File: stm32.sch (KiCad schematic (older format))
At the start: 35 parts, among them J10 Micro_SD_Card, J16 Conn_02x20_Odd_Even, P2 CONN_01X04, U3 STM32F407VETx, U4 USBLC6-4SC6, Y2 25M, Y3 RTC

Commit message: add bodge pads and move stuff around
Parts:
- added TP1, TP10, TP11, TP2, TP3, TP4, TP5, TP6, TP7, TP8, TP9: TestPoint, TestPoint:TestPoint_Pad_D1.0mm, symbol Connector:TestPoint
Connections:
- net at U3.55 (PD8): now also TP3.1
- net at U3.56 (PD9): now also TP4.1
- net at U3.57 (PD10): now also TP5.1
- net at U3.58 (PD11): now also TP6.1
- net at U3.59 (PD12): now also TP7.1
- net at U3.61 (PD14): now also TP8.1
- net at U3.62 (PD15): now also TP9.1
- net at U3.63 (PC6): now also TP10.1
- net at U3.64 (PC7): now also TP11.1
- net at U3.68 (PA9): now also TP1.1
- net at U3.69 (PA10): now also TP2.1
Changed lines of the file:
@@
 	8700 1500 8750 1500
-$Comp
-L stmbl:STM32F40xV U3
-U 1 1 57A8F89A
-P 10100 3950
-F 0 "U3" H 10850 1200 50  0000 C CNN
-F 1 "STM32F407VETx" H 10100 3950 50  0000 C CNN
-F 2 "stmbl:LQFP-100_14x14mm_Pitch0.5mm" H 10100 3100 50  0001 C CNN
-F 3 "" H 10100 3950 50  0000 C CNN
-F 4 "" H 0   0   50  0001 C CNN "Manufacturer No"
-F 5 "" H 0   0   50  0001 C CNN "Source"
-F 6 "" H 0   0   50  0001 C CNN "Tolerance"
-F 7 "" H 0   0   50  0001 C CNN "Voltage"
-	1    10100 3950
-	1    0    0    -1
-$EndComp
 $Comp
 L stmbl:C C46
@@
 	1    0    0    -1
 $EndComp
+$Comp
+L stmbl:STM32F40xV U3
+U 1 1 57A8F89A
+P 10100 3950
+F 0 "U3" H 10850 1200 50  0000 C CNN
+F 1 "STM32F407VETx" H 10100 3950 50  0000 C CNN
+F 2 "stmbl:LQFP-100_14x14mm_Pitch0.5mm" H 10100 3100 50  0001 C CNN
+F 3 "" H 10100 3950 50  0000 C CNN
+F 4 "" H 0   0   50  0001 C CNN "Manufacturer No"
+F 5 "" H 0   0   50  0001 C CNN "Source"
+F 6 "" H 0   0   50  0001 C CNN "Tolerance"
+F 7 "" H 0   0   50  0001 C CNN "Voltage"
+	1    10100 3950
+	1    0    0    -1
+$EndComp
+$Comp
+L Connector:TestPoint TP3
+U 1 1 5D2700EF
+P 11400 4000
+F 0 "TP3" V 11354 4188 50  0000 L CNN
+F 1 "TestPoint" V 11400 4300 50  0000 L CNN
+F 2 "TestPoint:TestPoint_Pad_D1.0mm" H 11600 4000 50  0001 C CNN
+F 3 "~" H 11600 4000 50  0001 C CNN
+	1    11400 4000
+	0    1    1    0
+$EndComp
+Wire Wire Line
+	11250 4000 11400 4000
+$Comp
+L Connector:TestPoint TP4
+U 1 1 5D2704C1
+P 11400 4100
+F 0 "TP4" V 11354 4288 50  0000 L CNN
+F 1 "TestPoint" V 11400 4400 50  0000 L CNN
+F 2 "TestPoint:TestPoint_Pad_D1.0mm" H 11600 4100 50  0001 C CNN
+F 3 "~" H 11600 4100 50  0001 C CNN
+	1    11400 4100
+	0    1    1    0
+$EndComp
+Wire Wire Line
+	11250 4100 11400 4100
+$Comp
+L Connector:TestPoint TP5
+U 1 1 5D270727
+P 11400 4200
+F 0 "TP5" V 11354 4388 50  0000 L CNN
+F 1 "TestPoint" V 11400 4500 50  0000 L CNN
+F 2 "TestPoint:TestPoint_Pad_D1.0mm" H 11600 4200 50  0001 C CNN
+F 3 "~" H 11600 4200 50  0001 C CNN
+	1    11400 4200
+	0    1    1    0
+$EndComp
+Wire Wire Line
+	11250 4200 11400 4200
+$Comp
+L Connector:TestPoint TP6
+U 1 1 5D2709E1
+P 11400 4300
+F 0 "TP6" V 11354 4488 50  0000 L CNN
+F 1 "TestPoint" V 11400 4600 50  0000 L CNN
+F 2 "TestPoint:TestPoint_Pad_D1.0mm" H 11600 4300 50  0001 C CNN
+F 3 "~" H 11600 4300 50  0001 C CNN
+	1    11400 4300
+	0    1    1    0
+$EndComp
+Wire Wire Line
+	11250 4300 11400 4300
+$Comp
+L Connector:TestPoint TP7
+U 1 1 5D270C47
+P 11400 4400
+F 0 "TP7" V 11354 4588 50  0000 L CNN
+F 1 "TestPoint" V 11400 4700 50  0000 L CNN
+F 2 "TestPoint:TestPoint_Pad_D1.0mm" H 11600 4400 50  0001 C CNN
+F 3 "~" H 11600 4400 50  0001 C CNN
+	1    11400 4400
+	0    1    1    0
+$EndComp
+Wire Wire Line
+	11250 4400 11400 4400
+$Comp
+L Connector:TestPoint TP8
+U 1 1 5D270E75
+P 11400 4600
+F 0 "TP8" V 11354 4788 50  0000 L CNN
+F 1 "TestPoint" V 11400 4900 50  0000 L CNN
+F 2 "TestPoint:TestPoint_Pad_D1.0mm" H 11600 4600 50  0001 C CNN
+F 3 "~" H 11600 4600 50  0001 C CNN
+	1    11400 4600
+	0    1    1    0
+$EndComp
+Wire Wire Line
+	11250 4600 11400 4600
+$Comp
+L Connector:TestPoint TP9
+U 1 1 5D2710F7
+P 11400 4700
+F 0 "TP9" V 11354 4888 50  0000 L CNN
+F 1 "TestPoint" V 11400 5000 50  0000 L CNN
+F 2 "TestPoint:TestPoint_Pad_D1.0mm" H 11600 4700 50  0001 C CNN
+F 3 "~" H 11600 4700 50  0001 C CNN
+	1    11400 4700
+	0    1    1    0
+$EndComp
+Wire Wire Line
+	11250 4700 11400 4700
+$Comp
+L Connector:TestPoint TP10
+U 1 1 5D27230B
+P 11400 5600
+F 0 "TP10" V 11354 5788 50  0000 L CNN
+F 1 "TestPoint" V 11400 5900 50  0000 L CNN
+F 2 "TestPoint:TestPoint_Pad_D1.0mm" H 11600 5600 50  0001 C CNN
+F 3 "~" H 11600 5600 50  0001 C CNN
+	1    11400 5600
+	0    1    1    0
+$EndComp
+Wire Wire Line
+	11250 5600 11400 5600
+$Comp
+L Connector:TestPoint TP11
+U 1 1 5D2727D7
+P 11400 5700
+F 0 "TP11" V 11354 5888 50  0000 L CNN
+F 1 "TestPoint" V 11400 6000 50  0000 L CNN
+F 2 "TestPoint:TestPoint_Pad_D1.0mm" H 11600 5700 50  0001 C CNN
+F 3 "~" H 11600 5700 50  0001 C CNN
+	1    11400 5700
+	0    1    1    0
+$EndComp
+Wire Wire Line
+	11250 5700 11400 5700
+$Comp
+L Connector:TestPoint TP1
+U 1 1 5D272AB9
+P 8800 4100
+F 0 "TP1" V 8754 4288 50  0000 L CNN
+F 1 "TestPoint" V 8800 4400 50  0000 L CNN
+F 2 "TestPoint:TestPoint_Pad_D1.0mm" H 9000 4100 50  0001 C CNN
+F 3 "~" H 9000 4100 50  0001 C CNN
+	1    8800 4100
+	0    -1   -1   0
+$EndComp
+Wire Wire Line
+	8950 4100 8800 4100
+$Comp
+L Connector:TestPoint TP2
+U 1 1 5D272FE7
+P 8800 4200
+F 0 "TP2" V 8754 4388 50  0000 L CNN
+F 1 "TestPoint" V 8800 4500 50  0000 L CNN
+F 2 "TestPoint:TestPoint_Pad_D1.0mm" H 9000 4200 50  0001 C CNN
+F 3 "~" H 9000 4200 50  0001 C CNN
+	1    8800 4200
+	0    -1   -1   0
+$EndComp
+Wire Wire Line
+	8950 4200 8800 4200
 $EndSCHEMATC

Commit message: fix SD card socket, move around psu stuff
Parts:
- J10: footprint Connector_Card:microSD_HC_Hirose_DM3D-SF -> Connector_Card:microSD_HC_Hirose_DM3BT-DSF-PEJS
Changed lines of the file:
@@
 EESchema Schematic File Version 5
 LIBS:powermetering-cache
-EELAYER 29 0
+EELAYER 30 0
 EELAYER END
 $Descr A3 16535 11693
@@
 Comment3 ""
 Comment4 ""
+Comment5 ""
+Comment6 ""
+Comment7 ""
+Comment8 ""
+Comment9 ""
 $EndDescr
 Text HLabel 7850 3400 0    60   Input ~ 0
@@
 F 0 "J10" H 13500 6217 50  0000 C CNN
 F 1 "Micro_SD_Card" H 13500 6126 50  0000 C CNN
-F 2 "Connector_Card:microSD_HC_Hirose_DM3D-SF" H 14700 5800 50  0001 C CNN
+F 2 "Connector_Card:microSD_HC_Hirose_DM3BT-DSF-PEJS" H 14700 5800 50  0001 C CNN
 F 3 "http://katalog.we-online.de/em/datasheet/693072010801.pdf" H 13550 5500 50  0001 C CNN
 	1    13550 5500

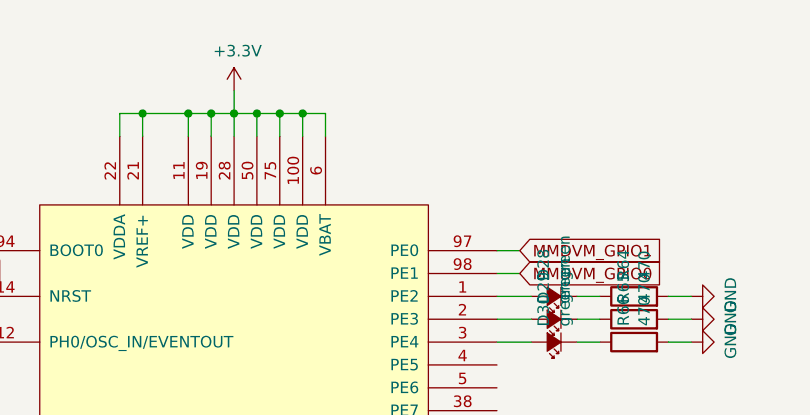
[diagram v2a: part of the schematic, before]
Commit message: remove eight pulse rectifier, add three pulse rectifier with artificial star point
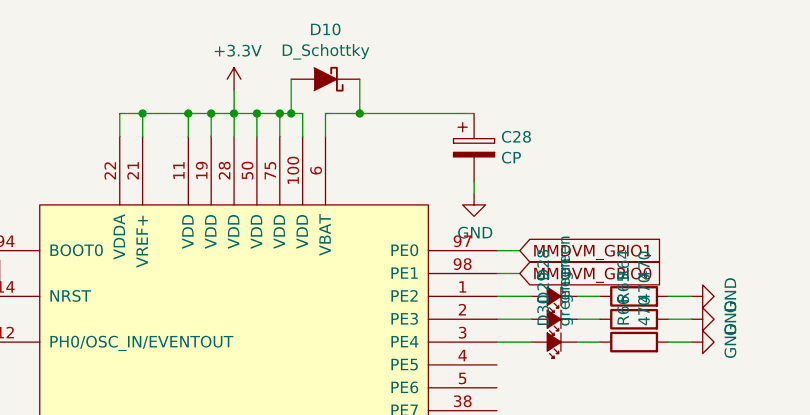
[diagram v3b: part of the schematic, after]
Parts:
- added C28: CP, symbol Device:CP
- added D10: D_Schottky, symbol stmbl:D_Schottky
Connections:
- net +3V3: now also D10.2 (A); no longer U3.6 (VBAT)
- net GND: now also C28.2
- new net: C28.1, D10.1 (K), U3.6 (VBAT)
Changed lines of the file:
@@
 EESchema Schematic File Version 5
-LIBS:powermetering-cache
 EELAYER 30 0
 EELAYER END
@@
 Connection ~ 10300 800
 Wire Wire Line
-	10300 800  10400 800
+	10300 800  10350 800
 Wire Wire Line
 	10200 900  10200 800
@@
 Wire Wire Line
 	12850 950  13100 950
-Wire Wire Line
-	10500 800  10400 800
-Connection ~ 10400 800
 Connection ~ 14600 950
 Wire Wire Line
@@
 Wire Wire Line
 	8950 4200 8800 4200
+$Comp
+L Device:CP C28
+U 1 1 5E135587
+P 11150 950
+F 0 "C28" H 11268 996 50  0000 L CNN
+F 1 "CP" H 11268 905 50  0000 L CNN
+F 2 "" H 11188 800 50  0001 C CNN
+F 3 "~" H 11150 950 50  0001 C CNN
+	1    11150 950
+	1    0    0    -1
+$EndComp
+$Comp
+L stmbl:D_Schottky D10
+U 1 1 5E135FC5
+P 10500 650
+F 0 "D10" H 10500 434 50  0000 C CNN
+F 1 "D_Schottky" H 10500 525 50  0000 C CNN
+F 2 "" H 10500 650 50  0000 C CNN
+F 3 "" H 10500 650 50  0000 C CNN
+	1    10500 650
+	-1   0    0    1
+$EndComp
+Wire Wire Line
+	10500 800  10650 800
+Wire Wire Line
+	10650 650  10650 800
+Connection ~ 10650 800
+Wire Wire Line
+	10650 800  11150 800
+Wire Wire Line
+	10350 650  10350 800
+Connection ~ 10350 800
+Wire Wire Line
+	10350 800  10400 800
+$Comp
+L stmbl:GND #PWR0153
+U 1 1 5E13711E
+P 11150 1150
+F 0 "#PWR0153" H 11150 900 50  0001 C CNN
+F 1 "GND" H 11155 977 50  0000 C CNN
+F 2 "" H 11150 1150 50  0000 C CNN
+F 3 "" H 11150 1150 50  0000 C CNN
+	1    11150 1150
+	1    0    0    -1
+$EndComp
+Wire Wire Line
+	11150 1150 11150 1100
 $EndSCHEMATC
